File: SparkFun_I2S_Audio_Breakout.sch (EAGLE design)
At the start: 20 parts, among them IC1 MAX98375A

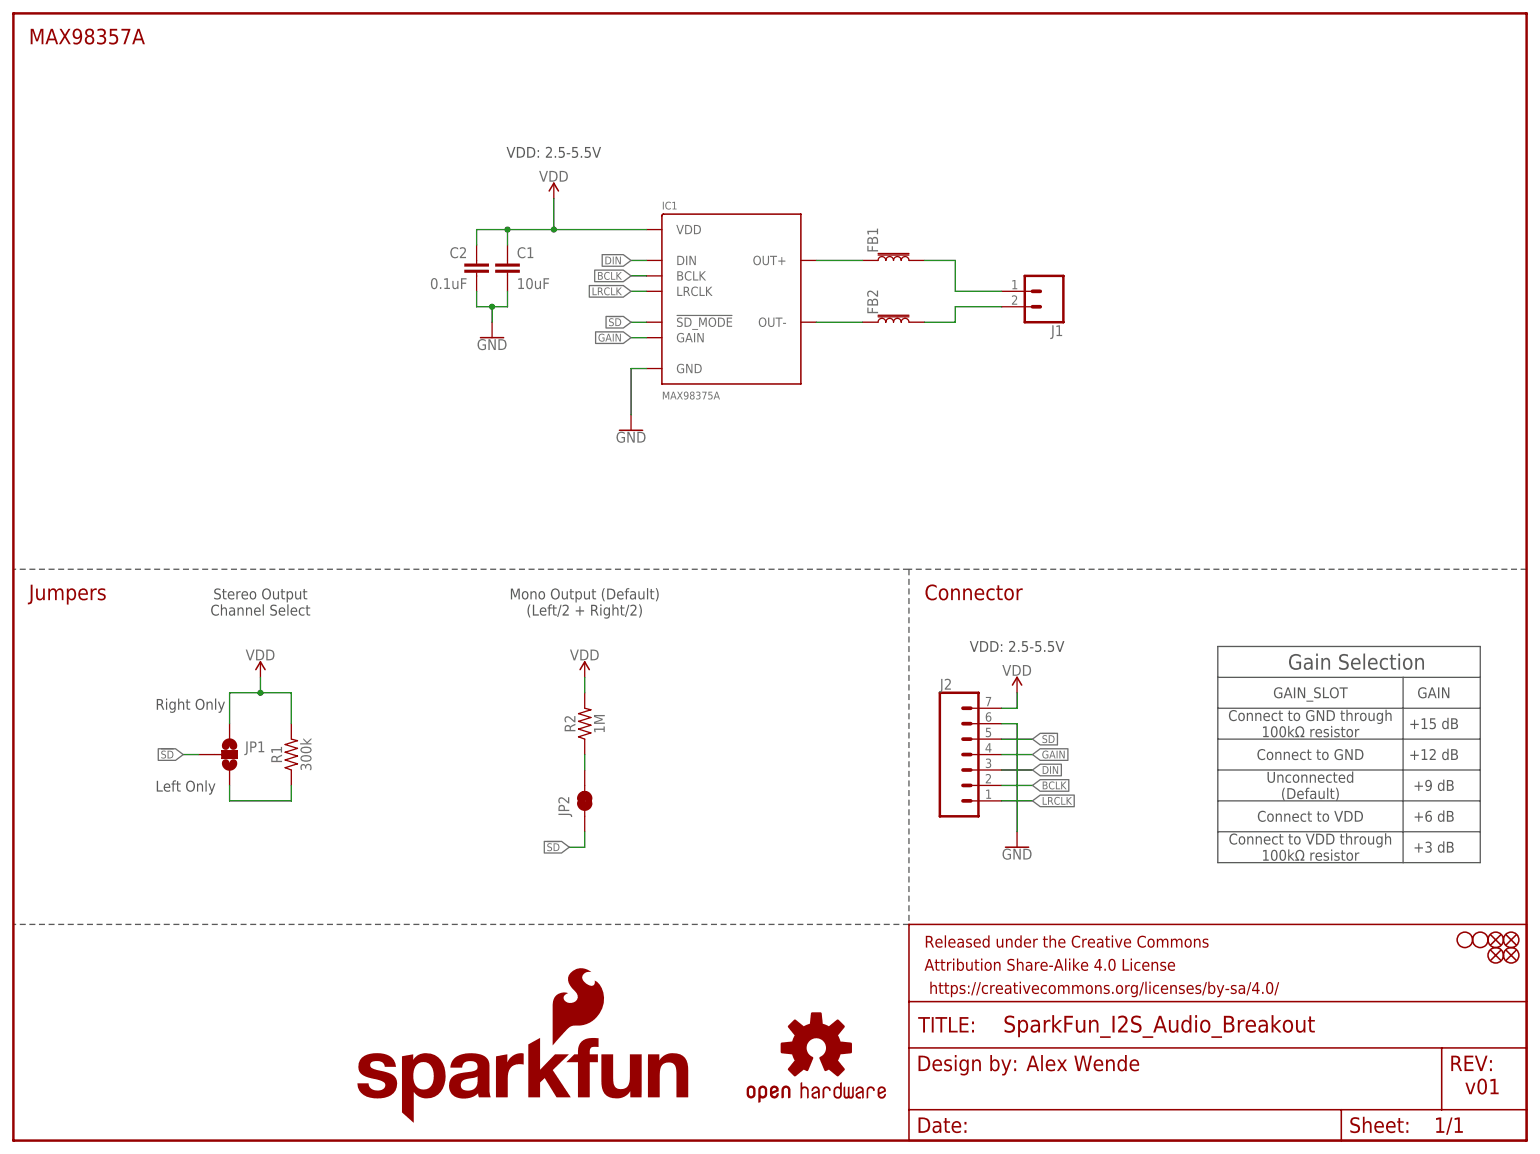
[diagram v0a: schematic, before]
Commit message: v10
Removed + symbol on top copper
Removed ferrite beads
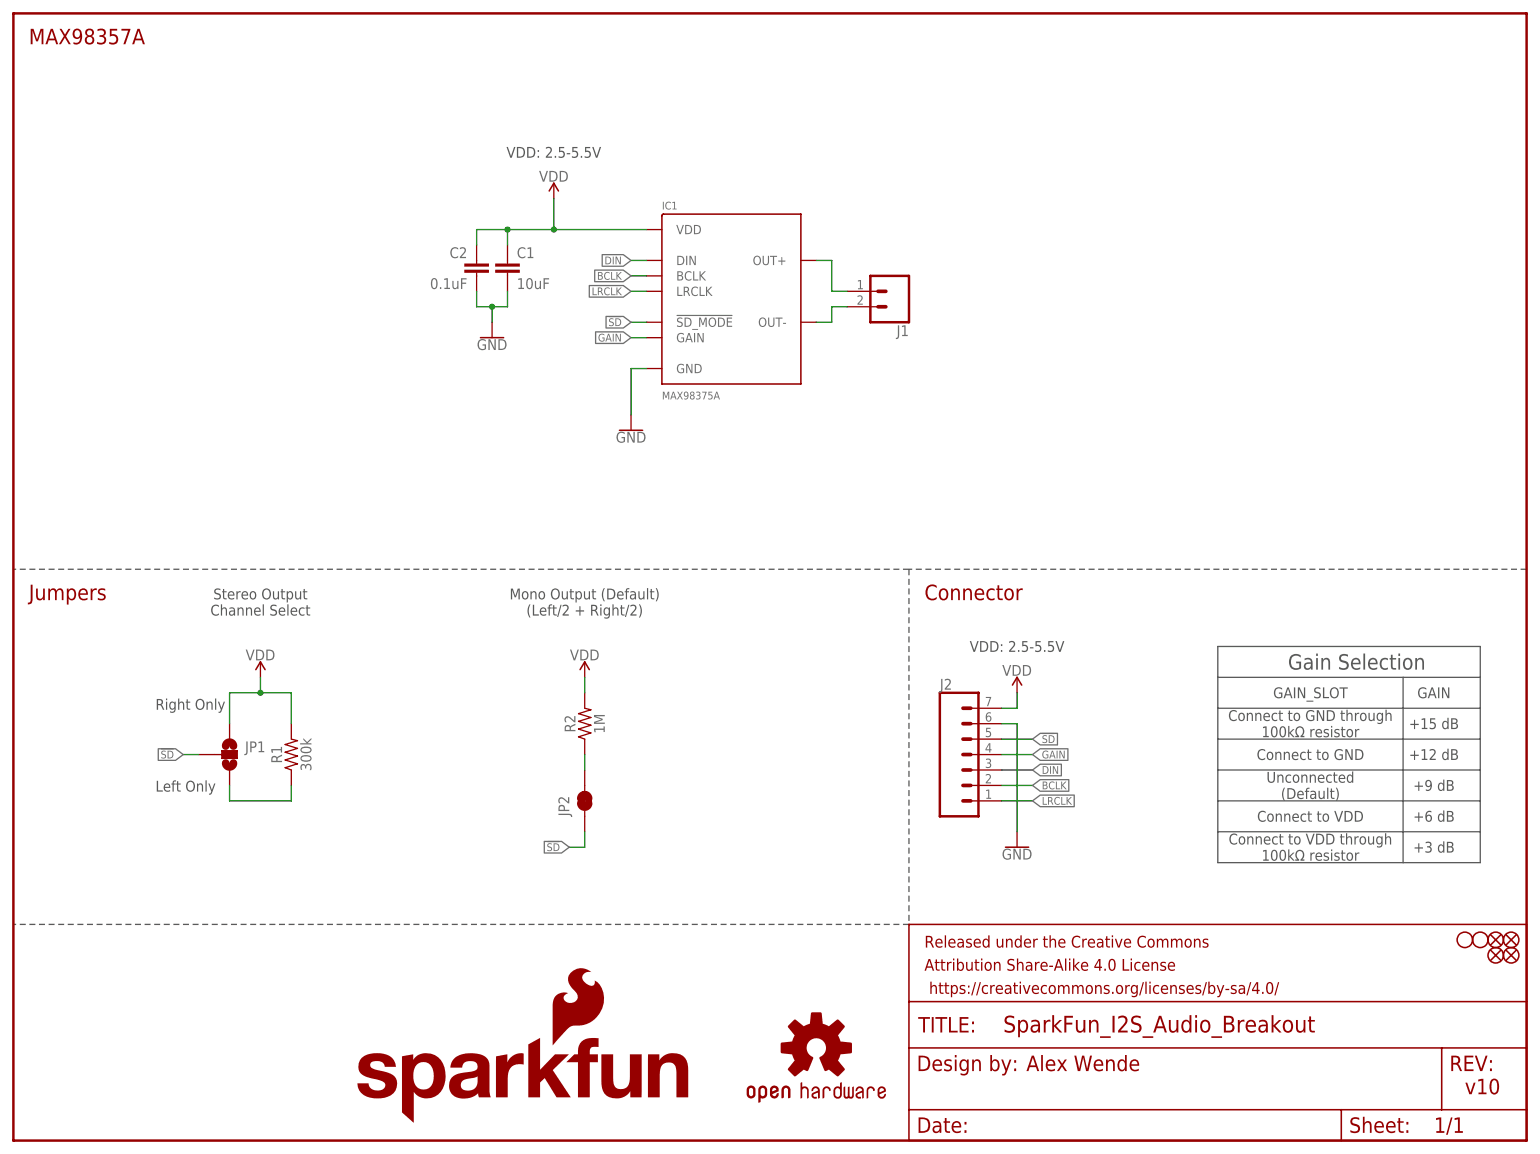
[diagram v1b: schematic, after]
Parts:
- removed FB1, FB2: FERRITE_BEAD-0603, SparkFun-Coils:FERRITE_BEAD-0603
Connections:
- removed net N$1: FB1.1, IC1.OUT+
- removed net N$2: FB2.1, IC1.OUT-
- removed net N$3: FB1.2, J1.1
- removed net N$4: FB2.2, J1.2
- new net OUT+: IC1.OUT+, J1.1
- new net OUT-: IC1.OUT-, J1.2
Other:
- note added: "v10"
- note removed: "v01"
- moved on the sheet: J1
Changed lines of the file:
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@@
 <?xml version="1.0" encoding="utf-8"?>
 <!DOCTYPE eagle SYSTEM "eagle.dtd">
-<eagle version="9.0.1">
+<eagle version="9.1.1">
 <drawing>
 <settings>
@@
 <part name="C1" library="SparkFun-Capacitors" deviceset="10UF" device="-0805-10V-10%" value="10uF"/>
 <part name="C2" library="SparkFun-Capacitors" deviceset="0.1UF" device="-0603-25V-(+80/-20%)" value="0.1uF"/>
-<part name="FB1" library="SparkFun-Coils" deviceset="FERRITE_BEAD" device="-0603" value=""/>
-<part name="FB2" library="SparkFun-Coils" deviceset="FERRITE_BEAD" device="-0603" value=""/>
 <part name="R1" library="SparkFun-Resistors" deviceset="300KOHM" device="-0603-1/10W-1%" value="300k"/>
 <part name="R2" library="SparkFun-Resistors" deviceset="1MOHM" device="-0603-1/4W-5%" value="1M"/>
@@
 <plain>
 <text x="166.624" y="11.43" size="2.54" layer="94" font="vector">Alex Wende</text>
-<text x="238.76" y="7.62" size="2.54" layer="94" font="vector">v01</text>
+<text x="238.76" y="7.62" size="2.54" layer="94" font="vector">v10</text>
 <wire x1="248.92" y1="93.98" x2="147.32" y2="93.98" width="0.1524" layer="97" style="longdash"/>
 <wire x1="147.32" y1="93.98" x2="147.32" y2="35.56" width="0.1524" layer="97" style="longdash"/>
@@
 <text x="40.64" y="86.36" size="1.778" layer="97" font="vector" align="bottom-center">Stereo Output
 Channel Select</text>
-<text x="220.98" y="78.74" size="2.54" layer="97" font="vector" align="center">Gain Selection</text>
-<text x="213.36" y="68.58" size="1.778" layer="97" font="vector" align="center">Connect to GND through
+<text x="220.98" y="78.74" size="2.54" layer="97" align="center">Gain Selection</text>
+<text x="213.36" y="68.58" size="1.778" layer="97" align="center">Connect to GND through
 100kΩ resistor</text>
-<text x="213.36" y="63.5" size="1.778" layer="97" font="vector" align="center">Connect to GND</text>
-<text x="213.36" y="58.42" size="1.778" layer="97" font="vector" align="center">Unconnected
+<text x="213.36" y="63.5" size="1.778" layer="97" align="center">Connect to GND</text>
+<text x="213.36" y="58.42" size="1.778" layer="97" align="center">Unconnected
 (Default)</text>
-<text x="213.36" y="53.34" size="1.778" layer="97" font="vector" align="center">Connect to VDD</text>
-<text x="213.36" y="48.26" size="1.778" layer="97" font="vector" align="center">Connect to VDD through
+<text x="213.36" y="53.34" size="1.778" layer="97" align="center">Connect to VDD</text>
+<text x="213.36" y="48.26" size="1.778" layer="97" align="center">Connect to VDD through
 100kΩ resistor</text>
-<text x="233.68" y="68.58" size="1.778" layer="97" font="vector" align="center">+15 dB</text>
-<text x="233.68" y="63.5" size="1.778" layer="97" font="vector" align="center">+12 dB</text>
-<text x="233.68" y="58.42" size="1.778" layer="97" font="vector" align="center">+9 dB</text>
-<text x="233.68" y="53.34" size="1.778" layer="97" font="vector" align="center">+6 dB</text>
-<text x="233.68" y="48.26" size="1.778" layer="97" font="vector" align="center">+3 dB</text>
+<text x="233.68" y="68.58" size="1.778" layer="97" align="center">+15 dB</text>
+<text x="233.68" y="63.5" size="1.778" layer="97" align="center">+12 dB</text>
+<text x="233.68" y="58.42" size="1.778" layer="97" align="center">+9 dB</text>
+<text x="233.68" y="53.34" size="1.778" layer="97" align="center">+6 dB</text>
+<text x="233.68" y="48.26" size="1.778" layer="97" align="center">+3 dB</text>
 <wire x1="198.12" y1="81.28" x2="198.12" y2="76.2" width="0.1524" layer="97"/>
 <wire x1="198.12" y1="76.2" x2="198.12" y2="71.12" width="0.1524" layer="97"/>
@@
 <wire x1="228.6" y1="76.2" x2="241.3" y2="76.2" width="0.1524" layer="97"/>
 <wire x1="228.6" y1="76.2" x2="228.6" y2="45.72" width="0.1524" layer="97"/>
-<text x="213.36" y="73.66" size="1.778" layer="97" font="vector" align="center">GAIN_SLOT</text>
-<text x="233.68" y="73.66" size="1.778" layer="97" font="vector" align="center">GAIN</text>
+<text x="213.36" y="73.66" size="1.778" layer="97" align="center">GAIN_SLOT</text>
+<text x="233.68" y="73.66" size="1.778" layer="97" align="center">GAIN</text>
 <wire x1="198.12" y1="71.12" x2="241.3" y2="71.12" width="0.1524" layer="97"/>
 <wire x1="198.12" y1="66.04" x2="241.3" y2="66.04" width="0.1524" layer="97"/>
@@
 <instance part="C1" gate="G$1" x="81.28" y="142.24"/>
 <instance part="C2" gate="G$1" x="76.2" y="142.24" rot="MR0"/>
-<instance part="FB1" gate="G$1" x="144.78" y="144.78" rot="R90"/>
-<instance part="FB2" gate="G$1" x="144.78" y="134.62" rot="R90"/>
 <instance part="R1" gate="G$1" x="45.72" y="63.5" rot="R90"/>
 <instance part="R2" gate="G$1" x="93.98" y="68.58" rot="R90"/>
-<instance part="J1" gate="G$1" x="170.18" y="139.7" rot="R180"/>
+<instance part="J1" gate="G$1" x="144.78" y="139.7" rot="R180"/>
 <instance part="JP1" gate="G$1" x="35.56" y="63.5"/>
 <instance part="SUPPLY1" gate="VDD" x="88.9" y="154.94"/>
@@
 </busses>
 <nets>
-<net name="N$1" class="0">
+<net name="OUT+" class="0">
 <segment>
 <pinref part="IC1" gate="G$1" pin="OUT+"/>
-<pinref part="FB1" gate="G$1" pin="1"/>
-<wire x1="132.08" y1="144.78" x2="139.7" y2="144.78" width="0.1524" layer="91"/>
+<wire x1="134.62" y1="144.78" x2="134.62" y2="139.7" width="0.1524" layer="91"/>
+<pinref part="J1" gate="G$1" pin="1"/>
+<wire x1="134.62" y1="139.7" x2="137.16" y2="139.7" width="0.1524" layer="91"/>
+<wire x1="132.08" y1="144.78" x2="134.62" y2="144.78" width="0.1524" layer="91"/>
 </segment>
 </net>
-<net name="N$2" class="0">
+<net name="OUT-" class="0">
 <segment>
 <pinref part="IC1" gate="G$1" pin="OUT-"/>
-<pinref part="FB2" gate="G$1" pin="1"/>
-<wire x1="132.08" y1="134.62" x2="139.7" y2="134.62" width="0.1524" layer="91"/>
+<wire x1="134.62" y1="134.62" x2="134.62" y2="137.16" width="0.1524" layer="91"/>
+<pinref part="J1" gate="G$1" pin="2"/>
+<wire x1="134.62" y1="137.16" x2="137.16" y2="137.16" width="0.1524" layer="91"/>
+<wire x1="132.08" y1="134.62" x2="134.62" y2="134.62" width="0.1524" layer="91"/>
 </segment>
 </net>
-<net name="N$3" class="0">
-<segment>
-<pinref part="FB1" gate="G$1" pin="2"/>
-<wire x1="149.86" y1="144.78" x2="154.94" y2="144.78" width="0.1524" layer="91"/>
-<wire x1="154.94" y1="144.78" x2="154.94" y2="139.7" width="0.1524" layer="91"/>
-<pinref part="J1" gate="G$1" pin="1"/>
-<wire x1="154.94" y1="139.7" x2="162.56" y2="139.7" width="0.1524" layer="91"/>
-</segment>
-</net>
-<net name="N$4" class="0">
-<segment>
-<pinref part="FB2" gate="G$1" pin="2"/>
-<wire x1="149.86" y1="134.62" x2="154.94" y2="134.62" width="0.1524" layer="91"/>
-<wire x1="154.94" y1="134.62" x2="154.94" y2="137.16" width="0.1524" layer="91"/>
-<pinref part="J1" gate="G$1" pin="2"/>
-<wire x1="154.94" y1="137.16" x2="162.56" y2="137.16" width="0.1524" layer="91"/>
-</segment>
-</net>

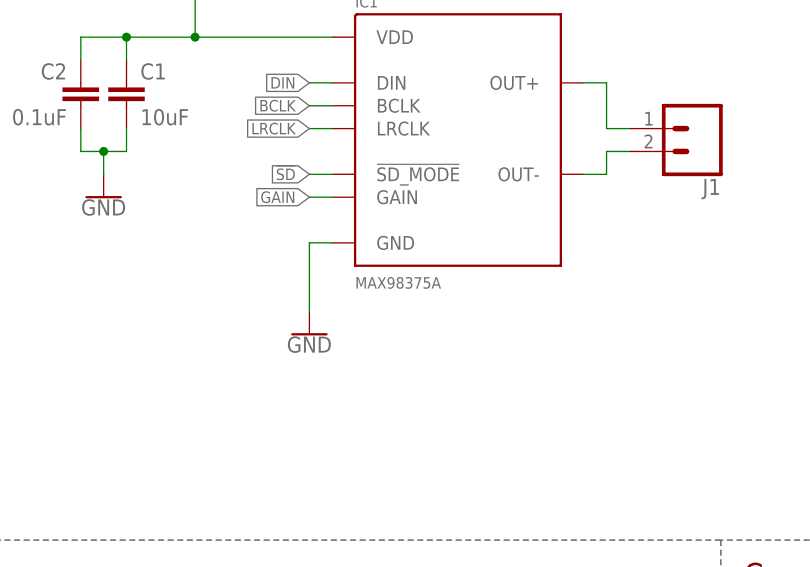
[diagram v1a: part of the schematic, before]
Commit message: Fixed IC1 Value
-Fixed IC1 value from MAX98375A to MAX98357A
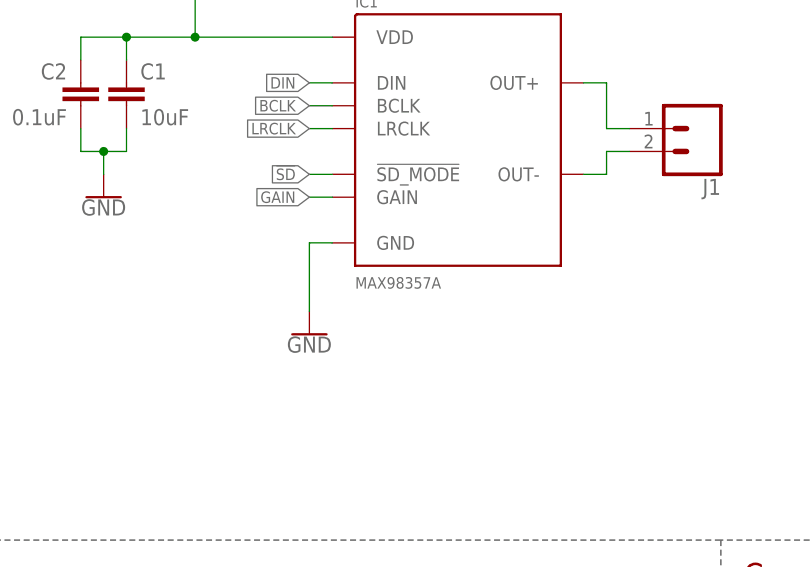
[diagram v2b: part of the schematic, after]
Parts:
- IC1: value MAX98375A -> MAX98357A
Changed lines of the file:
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@@
 </classes>
 <parts>
-<part name="IC1" library="SparkFun-IC-Amplifiers" deviceset="MAX98357A" device="" value="MAX98375A"/>
+<part name="IC1" library="SparkFun-IC-Amplifiers" deviceset="MAX98357A" device="" value="MAX98357A"/>
 <part name="C1" library="SparkFun-Capacitors" deviceset="10UF" device="-0805-10V-10%" value="10uF"/>
 <part name="C2" library="SparkFun-Capacitors" deviceset="0.1UF" device="-0603-25V-(+80/-20%)" value="0.1uF"/>
